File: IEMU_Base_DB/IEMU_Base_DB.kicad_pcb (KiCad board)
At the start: 2 copper layers, 51 x 29 mm, 12 parts, among them J1 USB_C_Receptacle_USB2.0_16P, J2 Conn_ARM_SWD_TagConnect_TC203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, J3 503398-1892, Q1 CSD85301Q2, U1 Ezurio BL54L15, U2 BQ29702DSER, U3 NPM1304-QEAA-R7, U4 USBLC6-2P6, U5 LSM6DSV320XTR, U6 MMC5603NJ

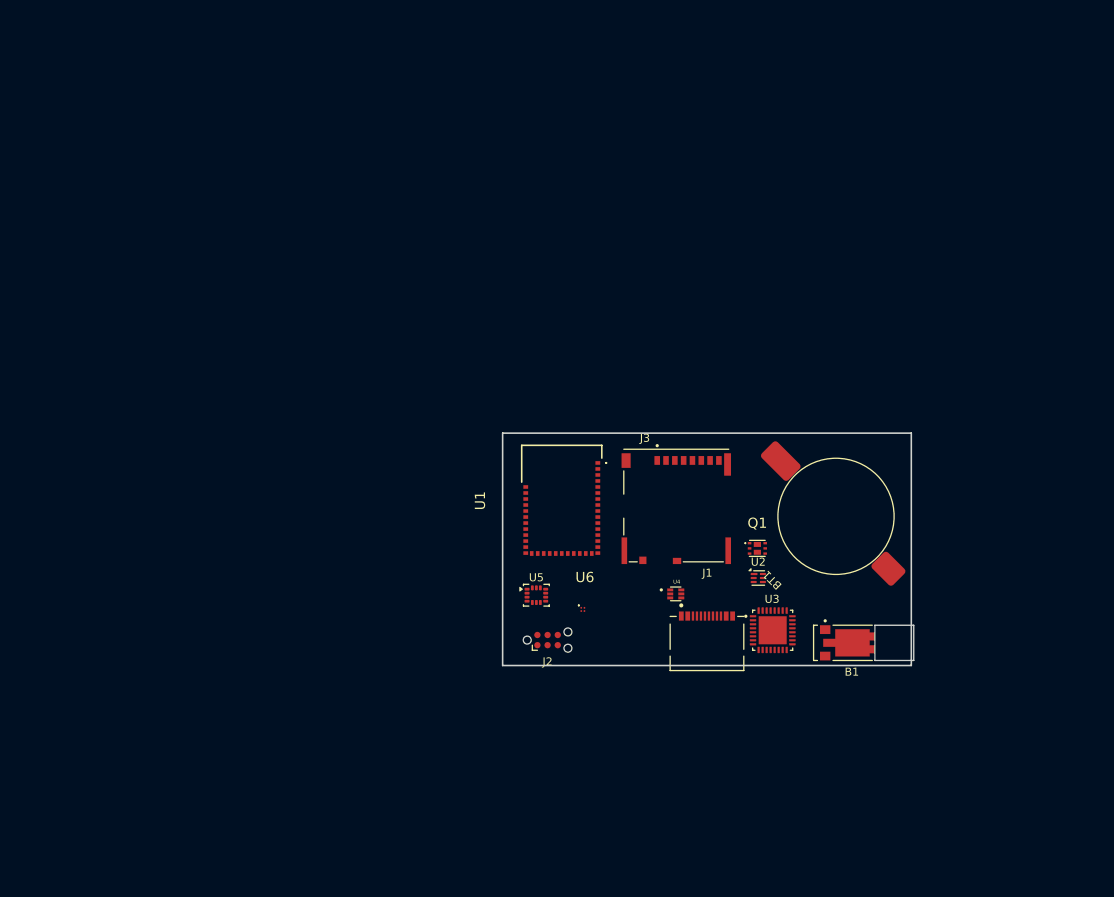
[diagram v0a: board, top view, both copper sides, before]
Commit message: layout of base and some fixes on the sensor layout
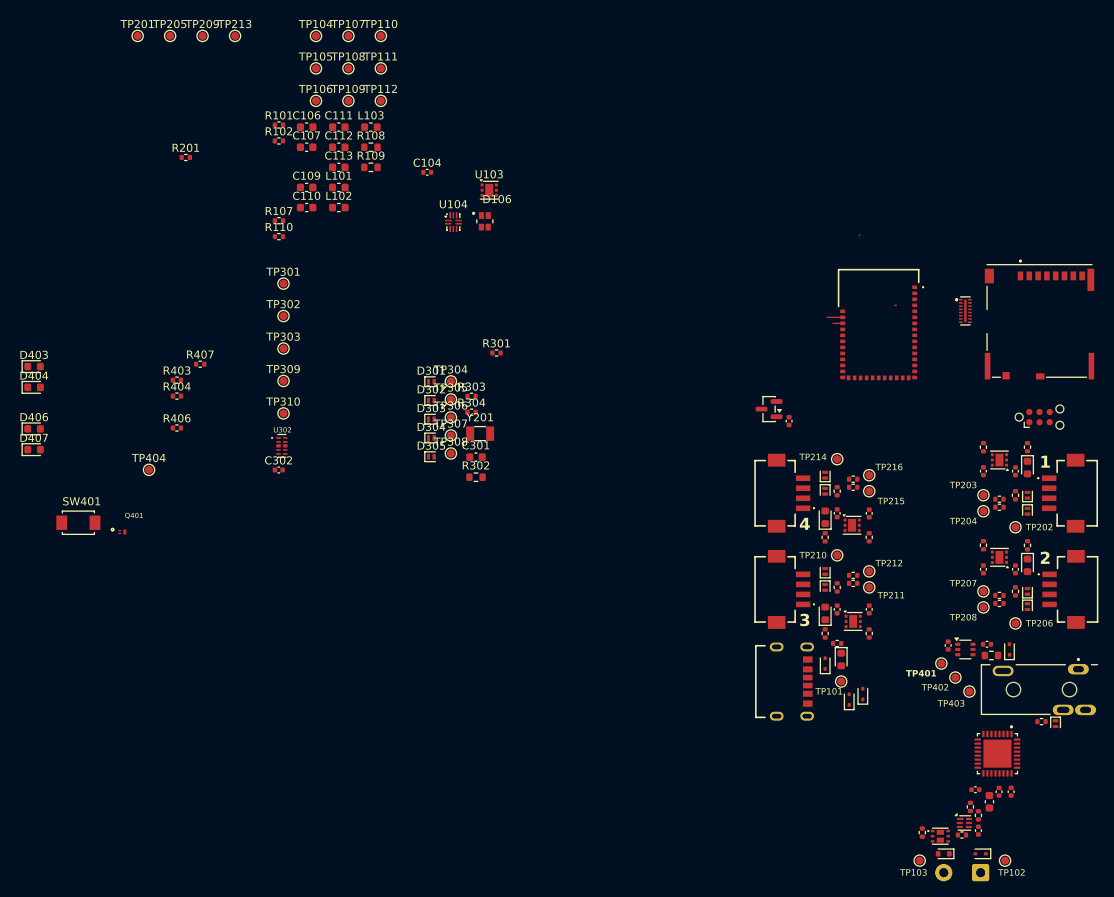
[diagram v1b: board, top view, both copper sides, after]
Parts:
- removed B1: VZ43FM1B8230001L, 0_Feedback:XDCR_VZ43FM1B8230001L
- removed BT1: Battery_Cell, 0_Power:CoinCell_LIR1455_LBY2
- removed J1: USB_C_Receptacle_USB2.0_16P, 0_Connectors:CONN_8p94X6p5X3p16_12L_GCC
- removed J2: Conn_ARM_SWD_TagConnect_TC2030-NL, Connector:Tag-Connect_TC2030-IDC-NL_2x03_P1.27mm_Vertical
- removed J3: 503398-1892, 0_Connectors:MOLEX_503398-1892
- removed Q1: CSD85301Q2, 0_Power:CSD85301Q2
- removed U1: Ezurio BL54L15, 0_MCU:BL54L15
- removed U2: BQ29702DSER, Package_SON:WSON-6_1.5x1.5mm_P0.5mm
- removed U3: NPM1304-QEAA-R7, 0_Power:QFN50P500X500X90-33N
- removed U4: USBLC6-2P6, 0_Power:SOT50P160X60-6N
- removed U5: LSM6DSV320XTR, Package_LGA:LGA-14_3x2.5mm_P0.5mm_LayoutBorder3x4y
- removed U6: MMC5603NJ, 0_Sensors:MMC5603NJ
- added C101: 1u, Capacitor_SMD:C_0402_1005Metric, F.Cu at (237.0, 152.8)
- added C102: 2u2, Capacitor_SMD:C_0402_1005Metric, F.Cu at (234.0, 152.5)
- added C103: 100n, Capacitor_SMD:C_0402_1005Metric, F.Cu at (234.4, 157.6)
- added C104: 100n, Capacitor_SMD:C_0402_1005Metric, F.Cu at (165.6, 75.5)
- added C105: 1u, Capacitor_SMD:C_0402_1005Metric, F.Cu at (238.5, 152.8)
- added C106: 10u, Capacitor_SMD:C_0603_1608Metric, F.Cu at (150.5, 69.8)
- added C107: 10u, Capacitor_SMD:C_0603_1608Metric, F.Cu at (150.5, 72.3)
- added C108: 10u, Capacitor_SMD:C_0603_1608Metric, F.Cu at (235.8, 154.0)
- added C109: 10u, Capacitor_SMD:C_0603_1608Metric, F.Cu at (150.5, 77.3)
- added C110: 10u, Capacitor_SMD:C_0603_1608Metric, F.Cu at (150.5, 79.8)
- added C111: 10u, Capacitor_SMD:C_0603_1608Metric, F.Cu at (154.6, 69.8)
- added C112: 10u, Capacitor_SMD:C_0603_1608Metric, F.Cu at (154.6, 72.3)
- added C113: 10u, Capacitor_SMD:C_0603_1608Metric, F.Cu at (154.6, 74.8)
- added C201: 100n, Capacitor_SMD:C_0402_1005Metric, F.Cu at (235.0, 112.8)
- added C202: 100n, Capacitor_SMD:C_0402_1005Metric, F.Cu at (239.0, 112.8)
- added C203: 100n, Capacitor_SMD:C_0402_1005Metric, F.Cu at (235.0, 125.0)
- added C204: 100n, Capacitor_SMD:C_0402_1005Metric, F.Cu at (239.0, 125.0)
- added C205: 100n, Capacitor_SMD:C_0402_1005Metric, F.Cu at (220.8, 130.0)
- added C206: 100n, Capacitor_SMD:C_0402_1005Metric, F.Cu at (216.8, 130.0)
- added C207: 100n, Capacitor_SMD:C_0402_1005Metric, F.Cu at (220.8, 118.0)
- added C208: 100n, Capacitor_SMD:C_0402_1005Metric, F.Cu at (216.8, 118.0)
- added C301: 10u, Capacitor_SMD:C_0603_1608Metric, F.Cu at (171.7, 111.0)
- added C302: 3p7, Capacitor_SMD:C_0402_1005Metric, F.Cu at (147.1, 112.6)
- added C401: 100n, Capacitor_SMD:C_0402_1005Metric, F.Cu at (230.6, 134.5)
- added C402: 100n, Capacitor_SMD:C_0402_1005Metric, F.Cu at (235.4, 134.3)
- added C403: 100n, Capacitor_SMD:C_0402_1005Metric, F.Cu at (210.8, 106.5)
- added D101: ESD5Z5.0T1G, Diode_SMD:D_SOD-523_1, F.Cu at (215.2, 136.8)
- added D102: ESD5Z5.0T1G, Diode_SMD:D_SOD-523_1, F.Cu at (219.9, 140.6)
- added D103: ESD5Z5.0T1G, Diode_SMD:D_SOD-523_1, F.Cu at (218.2, 141.2)
- added D104: ESD5Z5.0T1G, Diode_SMD:D_SOD-523_1, F.Cu at (234.7, 160.5)
- added D105: TPD1E10B06DYAR, Diode_SMD:D_SOD-523, F.Cu at (230.1, 160.5)
- added D106: LTST-C19HE1WT, 0_Feedback:LED_LTST-C19HE1WT, F.Cu at (172.8, 81.6)
- added D201: ESD9L1P8, Diode_SMD:D_SOD-882, F.Cu at (240.5, 115.8)
- added D202: ESD9L1P8, Diode_SMD:D_SOD-882, F.Cu at (240.5, 117.8)
- added D203: ESD9L1P8, Diode_SMD:D_SOD-882, F.Cu at (240.5, 127.8)
- added D204: ESD9L1P8, Diode_SMD:D_SOD-882, F.Cu at (240.5, 129.7)
- added D205: ESD9L1P8, Diode_SMD:D_SOD-882, F.Cu at (215.2, 127.2)
- added D206: ESD9L1P8, Diode_SMD:D_SOD-882, F.Cu at (215.2, 125.2)
- added D207: ESD9L1P8, Diode_SMD:D_SOD-882, F.Cu at (215.2, 115.2)
- added D208: ESD9L1P8, Diode_SMD:D_SOD-882, F.Cu at (215.2, 113.2)
- added D301: ESD9L1P8, Diode_SMD:D_SOD-882, F.Cu at (166.1, 101.6)
- added D302: ESD9L1P8, Diode_SMD:D_SOD-882, F.Cu at (166.1, 103.9)
- added D303: ESD9L1P8, Diode_SMD:D_SOD-882, F.Cu at (166.1, 106.3)
- added D304: ESD9L1P8, Diode_SMD:D_SOD-882, F.Cu at (166.1, 108.6)
- added D305: ESD9L1P8, Diode_SMD:D_SOD-882, F.Cu at (166.1, 110.9)
- added D401: ESD5Z5.0T1G, Diode_SMD:D_SOD-523_1, F.Cu at (238.2, 135.0)
- added D402: ESD9L1P8, Diode_SMD:D_SOD-882, F.Cu at (244.0, 144.2)
- added D403: LTST-C191KRKT, 0_Feedback:LTST-C191KRKT, F.Cu at (116.5, 99.7)
- added D404: LTST-C191KRKT, 0_Feedback:LTST-C191KRKT, F.Cu at (116.5, 102.3)
- added D405: LTST-C191KRKT, 0_Feedback:LTST-C191KRKT, F.Cu at (217.2, 136.2)
- added D406: LTST-C191KRKT, 0_Feedback:LTST-C191KRKT, F.Cu at (116.5, 107.5)
- added D407: LTST-C191KRKT, 0_Feedback:LTST-C191KRKT, F.Cu at (116.5, 110.1)
- added D408: LTST-C191KRKT, 0_Feedback:LTST-C191KRKT, F.Cu at (240.5, 112.3)
- added D409: LTST-C191KRKT, 0_Feedback:LTST-C191KRKT, F.Cu at (240.5, 124.5)
- added D410: LTST-C191KRKT, 0_Feedback:LTST-C191KRKT, F.Cu at (215.2, 130.5)
- added D411: LTST-C191KRKT, 0_Feedback:LTST-C191KRKT, F.Cu at (215.2, 118.5)
- added FL301: EMIF06-MSD02N16, 0_Connectors:EMIF06MSD02N16, F.Cu at (232.6, 92.8)
- added J101: USB4125-GF-A, 0_Connectors:GCT_USB4125-GF-A_REVA2, F.Cu at (210.0, 139.0)
- added J102: Conn_01x02_Pin, Connector_Wire:SolderWire-0.5sqmm_1x02_P4.6mm_D0.9mm_OD2.1mm, F.Cu at (234.7, 162.8)
- added J201: DF13-4P-1.25H(21), 0_Connectors:DF13-4P-1.25H(21), F.Cu at (246.7, 115.5)
- added J202: DF13-4P-1.25H(21), 0_Connectors:DF13-4P-1.25H(21), F.Cu at (246.8, 127.5)
- added J203: DF13-4P-1.25H(21), 0_Connectors:DF13-4P-1.25H(21), F.Cu at (209.0, 127.5)
- added J204: DF13-4P-1.25H(21), 0_Connectors:DF13-4P-1.25H(21), F.Cu at (209.0, 115.5)
- added J301: Conn_ARM_SWD_TagConnect_TC2030-NL, Connector:Tag-Connect_TC2030-IDC-NL_2x03_P1.27mm_Vertical, F.Cu at (242.0, 106.0)
- added J302: 503398-1892, 0_Connectors:MOLEX_503398-1892, F.Cu at (242.0, 94.0)
- added J401: SJ3-35083C-TR, 0_Connectors:SAMESKY_SJ3-35083C-TR, F.Cu at (242.2, 140.0)
- added L101: 2u2, Inductor_SMD:L_0603_1608Metric, F.Cu at (154.6, 77.3)
- added L102: 2u2, Inductor_SMD:L_0603_1608Metric, F.Cu at (154.6, 79.8)
- added L103: 2u2, Inductor_SMD:L_0603_1608Metric, F.Cu at (158.6, 69.8)
- added Q101: CSD85301Q2, 0_Power:CSD85301Q2, F.Cu at (229.6, 158.3)
- added Q401: CSD13381F4, 0_Power:DFN100X60X35-3N, F.Cu at (127.5, 120.3)
- added R101: 47k, Resistor_SMD:R_0402_1005Metric, F.Cu at (147.1, 69.5)
- added R102: 150k, Resistor_SMD:R_0402_1005Metric, F.Cu at (147.1, 71.5)
- added R103: 330, Resistor_SMD:R_0402_1005Metric, F.Cu at (234.4, 155.7)
- added R104: 1M, Resistor_SMD:R_0402_1005Metric, F.Cu at (232.3, 158.2)
- added R105: 1M, Resistor_SMD:R_0402_1005Metric, F.Cu at (227.4, 157.8)
- added R106: 2k2, Resistor_SMD:R_0402_1005Metric, F.Cu at (233.4, 154.7)
- added R107: 1M, Resistor_SMD:R_0402_1005Metric, F.Cu at (147.1, 81.5)
- added R108: 2M, Resistor_SMD:R_0603_1608Metric, F.Cu at (158.6, 72.3)
- added R109: 510k, Resistor_SMD:R_0603_1608Metric, F.Cu at (158.6, 74.8)
- added R110: R_Shunt_1R, Resistor_SMD:R_0402_1005Metric, F.Cu at (147.1, 83.5)
- added R201: 10k, Resistor_SMD:R_0402_1005Metric, F.Cu at (135.5, 73.6)
- added R202: 1M, Resistor_SMD:R_0402_1005Metric, F.Cu at (235.0, 109.8)
- added R203: 1k, Resistor_SMD:R_0402_1005Metric, F.Cu at (237.0, 116.2)
- added R204: 1k, Resistor_SMD:R_0402_1005Metric, F.Cu at (237.0, 117.2)
- added R205: 47k, Resistor_SMD:R_0402_1005Metric, F.Cu at (239.0, 115.8)
- added R206: 1M, Resistor_SMD:R_0402_1005Metric, F.Cu at (235.0, 122.0)
- added R207: 1k, Resistor_SMD:R_0402_1005Metric, F.Cu at (237.0, 128.2)
- added R208: 1k, Resistor_SMD:R_0402_1005Metric, F.Cu at (237.0, 129.2)
- added R209: 47k, Resistor_SMD:R_0402_1005Metric, F.Cu at (239.0, 127.8)
- added R210: 1M, Resistor_SMD:R_0402_1005Metric, F.Cu at (220.8, 133.0)
- added R211: 1k, Resistor_SMD:R_0402_1005Metric, F.Cu at (218.8, 126.8)
- added R212: 1k, Resistor_SMD:R_0402_1005Metric, F.Cu at (218.8, 125.8)
- added R213: 47k, Resistor_SMD:R_0402_1005Metric, F.Cu at (216.8, 127.2)
- added R214: 1M, Resistor_SMD:R_0402_1005Metric, F.Cu at (220.8, 121.0)
- added R215: 1k, Resistor_SMD:R_0402_1005Metric, F.Cu at (218.8, 114.8)
- added R216: 1k, Resistor_SMD:R_0402_1005Metric, F.Cu at (218.8, 113.8)
- added R217: 47k, Resistor_SMD:R_0402_1005Metric, F.Cu at (216.8, 115.2)
- added R301: 1k, Resistor_SMD:R_0402_1005Metric, F.Cu at (174.2, 98.0)
- added R302: 510k, Resistor_SMD:R_0603_1608Metric, F.Cu at (171.7, 113.5)
- added R303: 2k2, Resistor_SMD:R_0402_1005Metric, F.Cu at (171.1, 103.4)
- added R304: 2k2, Resistor_SMD:R_0402_1005Metric, F.Cu at (171.1, 105.4)
- added R401: 22R, Resistor_SMD:R_0603_1608Metric, F.Cu at (236.0, 135.8)
- added R402: 330R, Resistor_SMD:R_0402_1005Metric, F.Cu at (242.2, 144.0)
- added R403: 330R, Resistor_SMD:R_0402_1005Metric, F.Cu at (134.4, 101.4)
- added R404: 330R, Resistor_SMD:R_0402_1005Metric, F.Cu at (134.4, 103.4)
- added R405: 1k, Resistor_SMD:R_0402_1005Metric, F.Cu at (216.8, 134.2)
- added R406: 1k, Resistor_SMD:R_0402_1005Metric, F.Cu at (134.4, 107.4)
- added R407: 1k, Resistor_SMD:R_0402_1005Metric, F.Cu at (137.3, 99.4)
- added R408: 1k, Resistor_SMD:R_0402_1005Metric, F.Cu at (240.5, 109.8)
- added R409: 1k, Resistor_SMD:R_0402_1005Metric, F.Cu at (240.5, 122.0)
- added R410: 1k, Resistor_SMD:R_0402_1005Metric, F.Cu at (215.2, 133.0)
- added R411: 1k, Resistor_SMD:R_0402_1005Metric, F.Cu at (215.2, 121.0)
- added SW401: TS-1088-AR02016, 0_Feedback:SW_TS-1088-AR02016, F.Cu at (122.1, 119.2)
- added TP101: ~, TestPoint:TestPoint_Pad_D1.0mm, F.Cu at (217.2, 139.0)
- added TP102: ~, TestPoint:TestPoint_Pad_D1.0mm, F.Cu at (237.7, 161.3)
- added TP103: ~, TestPoint:TestPoint_Pad_D1.0mm, F.Cu at (227.1, 161.3)
- added TP104: ~, TestPoint:TestPoint_Pad_D1.0mm, F.Cu at (151.7, 58.4)
- added TP105: ~, TestPoint:TestPoint_Pad_D1.0mm, F.Cu at (151.7, 62.5)
- added TP106: ~, TestPoint:TestPoint_Pad_D1.0mm, F.Cu at (151.7, 66.5)
- added TP107: ~, TestPoint:TestPoint_Pad_D1.0mm, F.Cu at (155.8, 58.4)
- added TP108: ~, TestPoint:TestPoint_Pad_D1.0mm, F.Cu at (155.8, 62.5)
- added TP109: ~, TestPoint:TestPoint_Pad_D1.0mm, F.Cu at (155.8, 66.5)
- added TP110: ~, TestPoint:TestPoint_Pad_D1.0mm, F.Cu at (159.8, 58.4)
- added TP111: ~, TestPoint:TestPoint_Pad_D1.0mm, F.Cu at (159.8, 62.5)
- added TP112: ~, TestPoint:TestPoint_Pad_D1.0mm, F.Cu at (159.8, 66.5)
- added TP201: ~, TestPoint:TestPoint_Pad_D1.0mm, F.Cu at (129.5, 58.4)
- added TP202: ~, TestPoint:TestPoint_Pad_D1.0mm, F.Cu at (239.0, 119.8)
- added TP203: ~, TestPoint:TestPoint_Pad_D1.0mm, F.Cu at (235.0, 115.8)
- added TP204: ~, TestPoint:TestPoint_Pad_D1.0mm, F.Cu at (235.0, 117.8)
- added TP205: ~, TestPoint:TestPoint_Pad_D1.0mm, F.Cu at (133.5, 58.4)
- added TP206: ~, TestPoint:TestPoint_Pad_D1.0mm, F.Cu at (239.0, 131.8)
- added TP207: ~, TestPoint:TestPoint_Pad_D1.0mm, F.Cu at (235.0, 127.8)
- added TP208: ~, TestPoint:TestPoint_Pad_D1.0mm, F.Cu at (235.0, 129.8)
- added TP209: ~, TestPoint:TestPoint_Pad_D1.0mm, F.Cu at (137.6, 58.4)
- added TP210: ~, TestPoint:TestPoint_Pad_D1.0mm, F.Cu at (216.8, 123.2)
- added TP211: ~, TestPoint:TestPoint_Pad_D1.0mm, F.Cu at (220.8, 127.2)
- added TP212: ~, TestPoint:TestPoint_Pad_D1.0mm, F.Cu at (220.8, 125.2)
- added TP213: ~, TestPoint:TestPoint_Pad_D1.0mm, F.Cu at (141.6, 58.4)
- added TP214: ~, TestPoint:TestPoint_Pad_D1.0mm, F.Cu at (216.8, 111.2)
- added TP215: ~, TestPoint:TestPoint_Pad_D1.0mm, F.Cu at (220.8, 115.2)
- added TP216: ~, TestPoint:TestPoint_Pad_D1.0mm, F.Cu at (220.8, 113.2)
- added TP301: ~, TestPoint:TestPoint_Pad_D1.0mm, F.Cu at (147.7, 89.3)
- added TP302: ~, TestPoint:TestPoint_Pad_D1.0mm, F.Cu at (147.7, 93.4)
- added TP303: ~, TestPoint:TestPoint_Pad_D1.0mm, F.Cu at (147.7, 97.4)
- added TP304: TestPoint, TestPoint:TestPoint_Pad_D1.0mm, F.Cu at (168.5, 101.5)
- added TP305: TestPoint, TestPoint:TestPoint_Pad_D1.0mm, F.Cu at (168.5, 103.8)
- added TP306: TestPoint, TestPoint:TestPoint_Pad_D1.0mm, F.Cu at (168.5, 106.0)
- added TP307: TestPoint, TestPoint:TestPoint_Pad_D1.0mm, F.Cu at (168.5, 108.3)
- added TP308: TestPoint, TestPoint:TestPoint_Pad_D1.0mm, F.Cu at (168.5, 110.5)
- added TP309: ~, TestPoint:TestPoint_Pad_D1.0mm, F.Cu at (147.7, 101.5)
- added TP310: ~, TestPoint:TestPoint_Pad_D1.0mm, F.Cu at (147.7, 105.5)
- added TP401: ~, TestPoint:TestPoint_Pad_D1.0mm, F.Cu at (229.8, 136.8)
- added TP402: ~, TestPoint:TestPoint_Pad_D1.0mm, F.Cu at (231.5, 138.5)
- added TP403: ~, TestPoint:TestPoint_Pad_D1.0mm, F.Cu at (233.2, 140.2)
- added TP404: ~, TestPoint:TestPoint_Pad_D1.0mm, F.Cu at (130.9, 112.6)
- added U101: NPM1300-QEAA-R7, 0_Power:QFN50P500X500X90-33N, F.Cu at (236.8, 148.0)
- added U102: BQ29702DSER, Package_SON:WSON-6_1.5x1.5mm_P0.5mm, F.Cu at (232.6, 156.7)
- added U103: TPS61099DRV, Package_SON:WSON-6-1EP_2x2mm_P0.65mm_EP1x1.6mm, F.Cu at (173.3, 77.7)
- added U104: INA216A2RSWR, Package_DFN_QFN:Texas_RSW0010A_UQFN-10_1.4x1.8mm_P0.4mm, F.Cu at (168.9, 81.7)
- added U201: TPS2553DRVT, Package_SON:WSON-6-1EP_2x2mm_P0.65mm_EP1x1.6mm, F.Cu at (237.0, 111.3)
- added U202: TPS2553DRVT, Package_SON:WSON-6-1EP_2x2mm_P0.65mm_EP1x1.6mm, F.Cu at (237.0, 123.5)
- added U203: TPS2553DRVT, Package_SON:WSON-6-1EP_2x2mm_P0.65mm_EP1x1.6mm, F.Cu at (218.8, 131.5)
- added U204: TPS2553DRVT, Package_SON:WSON-6-1EP_2x2mm_P0.65mm_EP1x1.6mm, F.Cu at (218.6, 119.5)
- added U301: Ezurio BL54L15, 0_MCU:BL54L15, F.Cu at (221.9, 94.6)
- added U302: TMUX1204DQAR, 0_Switches:IC_TPD4EUSB30DQAR, F.Cu at (147.4, 109.6)
- added U401: SN74LVC1T45DCKR, Package_TO_SOT_SMD:SOT-363_SC-70-6, F.Cu at (232.8, 135.0)
- added U402: DRV5032FADBZR, Package_TO_SOT_SMD:SOT-23, F.Cu at (208.2, 105.0)
- added Y201: 32.768kHz, Crystal:Crystal_SMD_3215-2Pin_3.2x1.5mm, F.Cu at (172.2, 108.1)
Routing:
- net /3_nRF Module & SDCard/SPI_SD_CLK_MCU: track 0.00 -> 1.95 mm
- net /3_nRF Module & SDCard/SPI_SD_CS_MCU: track 0.00 -> 1.20 mm
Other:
- board outline removed
- copper layers 2 -> 4
- rule pad_to_mask_clearance: 0 -> 0.05
- board text added: "1"
- board text added: "2"
- board text added: "3"
- board text added: "4"
